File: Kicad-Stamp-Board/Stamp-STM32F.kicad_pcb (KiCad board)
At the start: 2 copper layers, 65 x 84 mm, 70 parts, among them J1 Conn_01x25, J2 Conn_01x25, J3 Conn_01x04, J4 BOOT1, SW1 Reset, SW2 BOOT, U1 STM32F103RET6, U2 ICL3221, Y1 32.768KHz

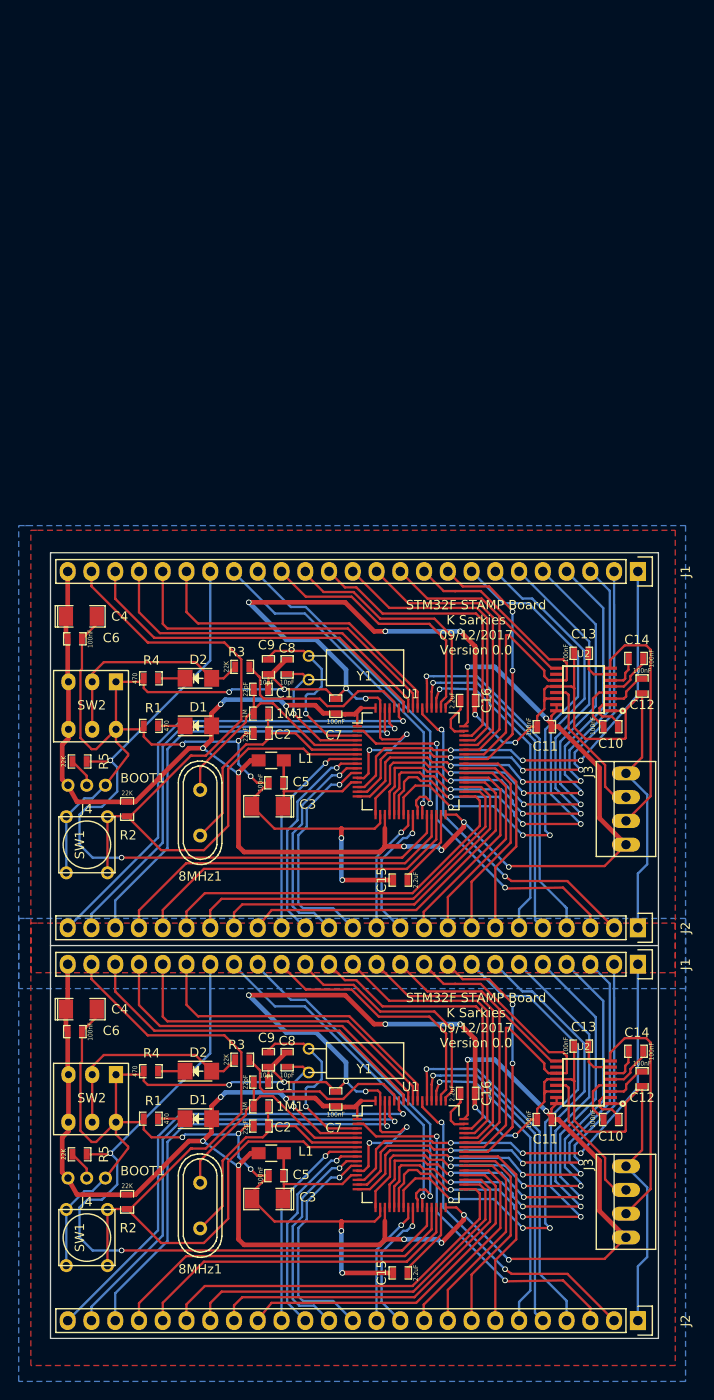
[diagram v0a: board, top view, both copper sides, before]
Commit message: Update PCB to allow more ground fill.
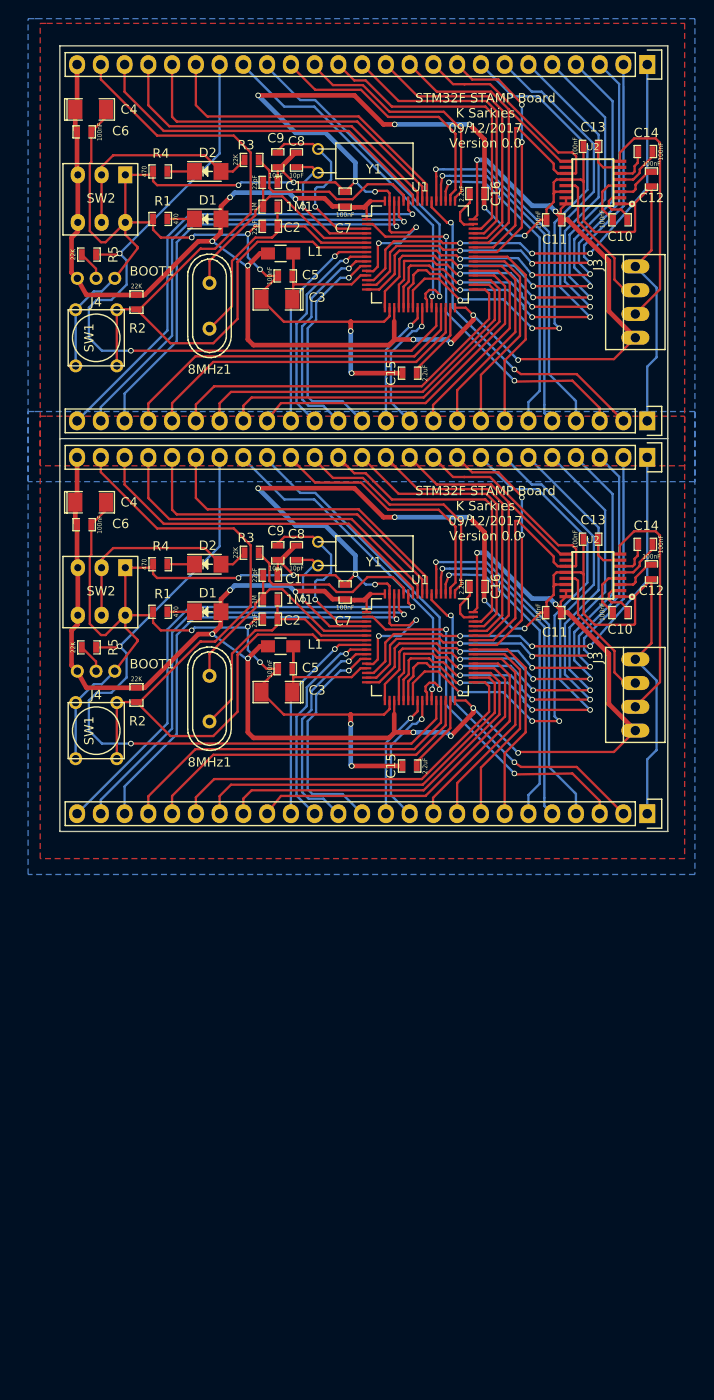
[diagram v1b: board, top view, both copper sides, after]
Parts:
- moved C7 54.2 mm to (145.5, 90.6)
- moved D2 54.2 mm to (130.8, 87.6)
- moved J3 54.2 mm to (176.5, 101.6)
- moved R2 54.2 mm to (123.2, 101.6)
- moved R4 54.2 mm to (125.7, 87.6)
- moved U2 54.2 mm to (172.0, 88.8)
- moved 8MHz1 54.2 mm to (131.0, 60.0)
- moved C1 54.2 mm to (137.5, 46.8)
- moved C1 54.2 mm to (137.5, 88.8)
- moved C10 54.2 mm to (174.9, 50.8)
- moved C10 54.2 mm to (174.9, 92.8)
- moved C11 54.2 mm to (167.8, 50.8)
- moved C11 54.2 mm to (167.8, 92.8)
- moved C12 54.2 mm to (178.2, 46.5)
- moved C12 54.2 mm to (178.2, 88.5)
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
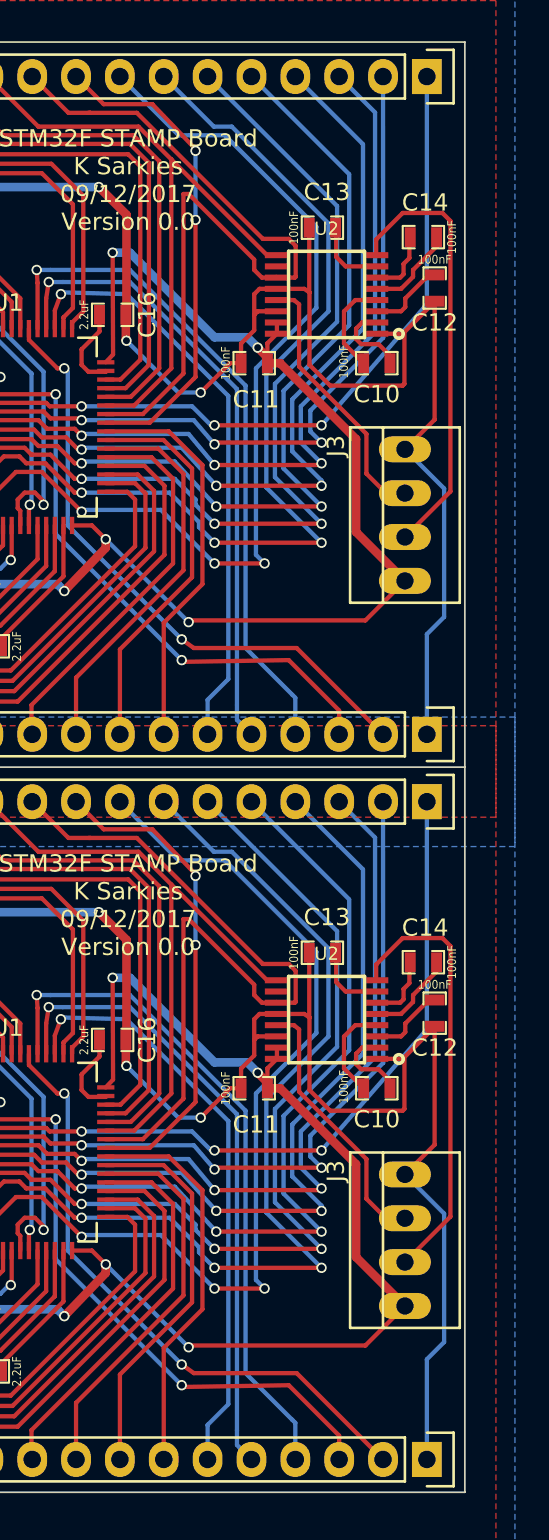
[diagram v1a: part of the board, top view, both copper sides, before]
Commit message: Fix SSOP-16 footprint plus some adjustments to PCB
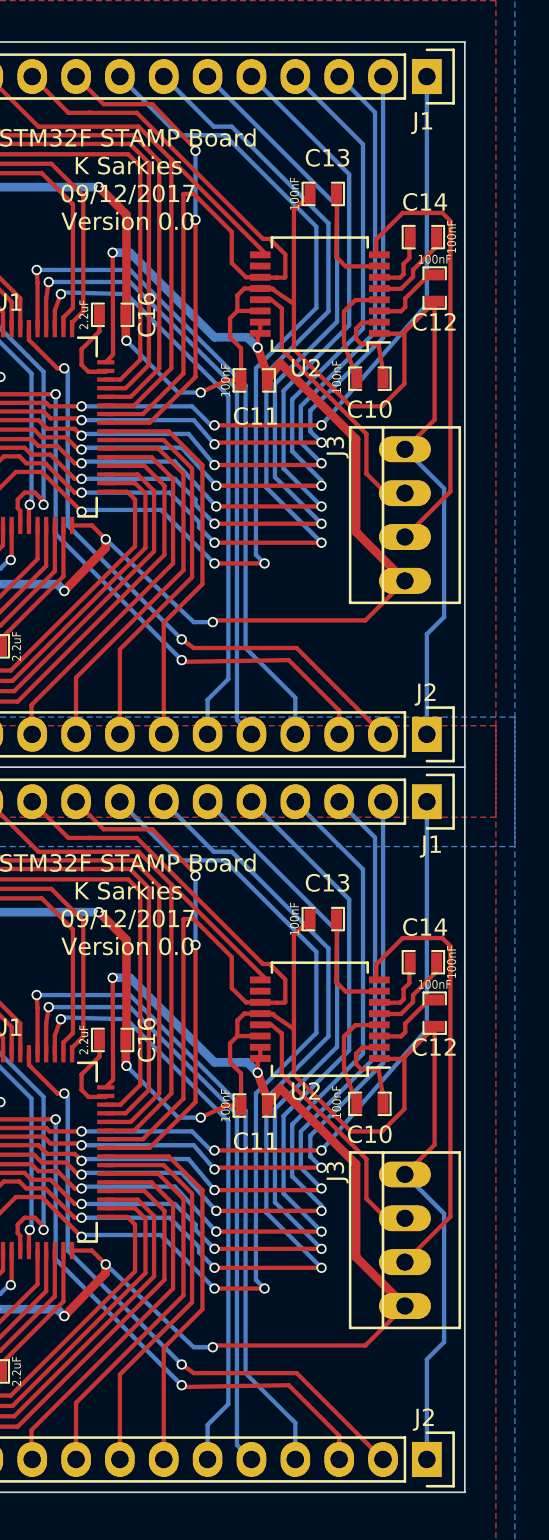
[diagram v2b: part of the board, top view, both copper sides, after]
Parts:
- removed the U2 at (172.0, 46.8)
- removed the U2 at (172.0, 88.8)
- added U2: ICL3221, stamp-stm32f:SSOP-16, F.Cu at (171.6, 46.8)
- added U2: ICL3221, stamp-stm32f:SSOP-16, F.Cu at (171.6, 88.8)
- moved C13 1.95 mm to (171.8, 41.0)
- moved C13 1.95 mm to (171.8, 83.0)
- moved C11 1.00 mm to (167.8, 51.8)
- moved C11 1.00 mm to (167.8, 93.8)
- moved C10 0.98 mm to (174.5, 51.7)
- moved C10 0.98 mm to (174.5, 93.7)
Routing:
- net Earth: track 535.8 -> 545.1 mm
- net Net-(C13-Pad2): track 8.67 -> 12.6 mm
- net PA9: track 92.1 -> 90.2 mm
- net Net-(C10-Pad1): track 9.42 -> 10.7 mm
- net PA10: track 75.6 -> 74.4 mm
- net Net-(C10-Pad2): track 11.2 -> 12.3 mm
- net Net-(J3-Pad3): track 32.1 -> 31.6 mm
